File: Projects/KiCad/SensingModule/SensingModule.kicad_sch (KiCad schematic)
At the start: 38 parts, among them J1 Conn_01x05_Socket, J2 Conn_01x02_Pin, J3 Conn_01x05_Pin, J4 Micro_SD_Card_Det_Hirose_DM3AT, SW1 SW_Push, SW2 SW_Push, U2 NUCLEO-F303K8, U4 MCP2562-E-P, U5 TLP222A, U6 MB85RS2MT, U7 MB85RS2MT

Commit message: 抵抗値を調整
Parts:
- R12, R13: value 100Ω -> 300Ω
- R14: value 1kΩ -> 300Ω
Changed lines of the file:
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@@
       (effects (font (size 1.27 1.27)) (justify left))
     )
-    (property "Value" "100Ω" (at 255.27 49.5299 0)
+    (property "Value" "300Ω" (at 255.27 49.5299 0)
       (effects (font (size 1.27 1.27)) (justify left))
     )
@@
       (effects (font (size 1.27 1.27)) (justify left))
     )
-    (property "Value" "100Ω" (at 245.11 49.5299 0)
+    (property "Value" "300Ω" (at 245.11 49.5299 0)
       (effects (font (size 1.27 1.27)) (justify left))
     )
@@
       (effects (font (size 1.27 1.27)) (justify left))
     )
-    (property "Value" "1kΩ" (at 265.43 49.5299 0)
-      (effects (font (size 1.27 1.27)) (justify left))
-    )
+    (property "Value" "300Ω" (at 265.43 49.5299 0)
+      (effects (font (size 1.27 1.27)) (justify left))
+    )

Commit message: リセッタブルフューズをSMDに変更
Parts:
- F1: footprint Fuse:Fuse_BelFuse_0ZRE0005FF_L8.3mm_W3.8mm -> Fuse:Fuse_1206_3216Metric_Pad1.42x1.75mm_HandSolder
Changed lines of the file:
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@@
       (effects (font (size 1.27 1.27)))
     )
-    (property "Footprint" "Fuse:Fuse_BelFuse_0ZRE0005FF_L8.3mm_W3.8mm" (at 154.94 74.93 0)
+    (property "Footprint" "Fuse:Fuse_1206_3216Metric_Pad1.42x1.75mm_HandSolder" (at 154.94 74.93 0)
       (effects (font (size 1.27 1.27)) (justify left) hide)
     )

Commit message: 一通り部品を選定
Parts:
- D1, D2: value LED -> ORANGE
- D3, D4: value LED -> GREEN
- D5, D6: value LED -> RED
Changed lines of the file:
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@@
       (effects (font (size 1.27 1.27)) (justify right))
     )
-    (property "Value" "LED" (at 256.54 61.2774 90)
+    (property "Value" "GREEN" (at 256.54 61.2774 90)
       (effects (font (size 1.27 1.27)) (justify right))
     )
@@
       (effects (font (size 1.27 1.27)) (justify right))
     )
-    (property "Value" "LED" (at 246.38 61.2774 90)
+    (property "Value" "GREEN" (at 246.38 61.2774 90)
       (effects (font (size 1.27 1.27)) (justify right))
     )
@@
       (effects (font (size 1.27 1.27)) (justify right))
     )
-    (property "Value" "LED" (at 276.86 61.2774 90)
+    (property "Value" "RED" (at 276.86 61.2774 90)
       (effects (font (size 1.27 1.27)) (justify right))
     )
@@
       (effects (font (size 1.27 1.27)) (justify right))
     )
-    (property "Value" "LED" (at 226.06 61.2774 90)
+    (property "Value" "ORANGE" (at 226.06 61.2774 90)
       (effects (font (size 1.27 1.27)) (justify right))
     )
@@
       (effects (font (size 1.27 1.27)) (justify right))
     )
-    (property "Value" "LED" (at 236.22 61.2774 90)
+    (property "Value" "ORANGE" (at 236.22 61.2774 90)
       (effects (font (size 1.27 1.27)) (justify right))
     )
@@
       (effects (font (size 1.27 1.27)) (justify right))
     )
-    (property "Value" "LED" (at 266.7 61.2774 90)
-      (effects (font (size 1.27 1.27)) (justify right))
-    )
+    (property "Value" "RED" (at 266.7 61.2774 90)
+      (effects (font (size 1.27 1.27)) (justify right))
+    )

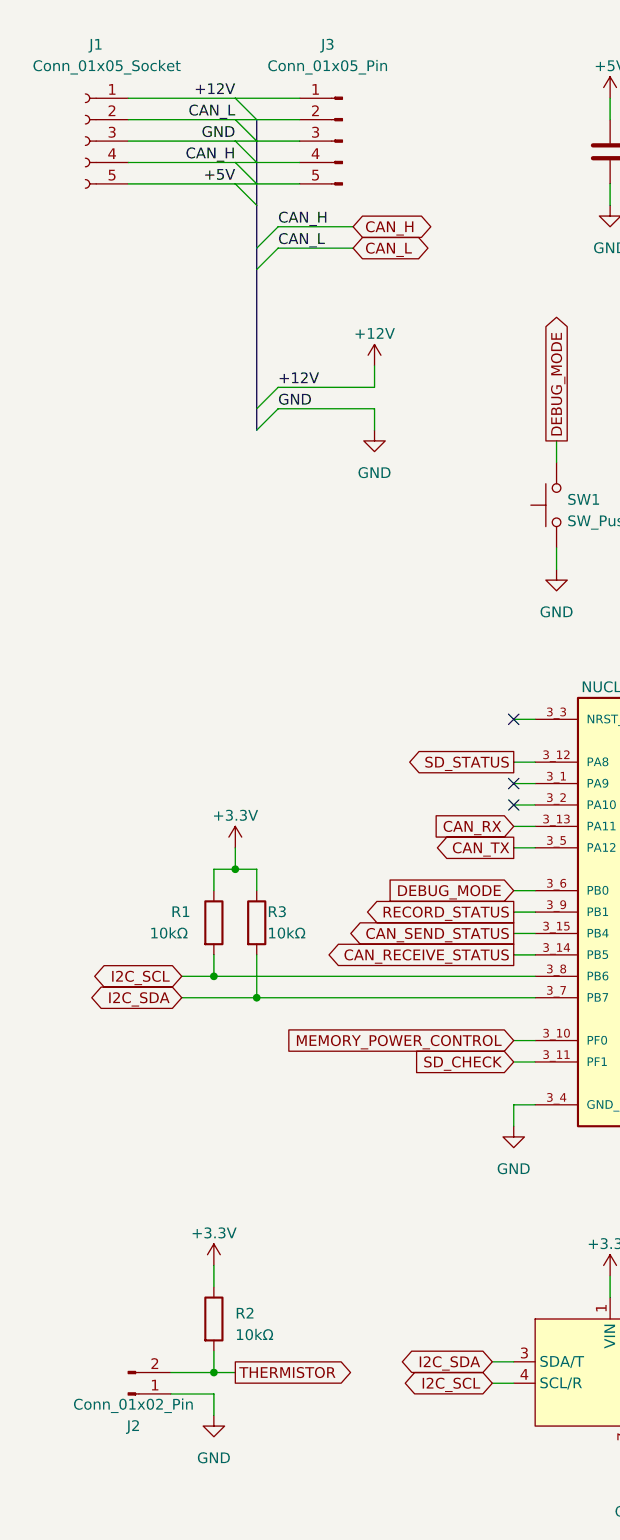
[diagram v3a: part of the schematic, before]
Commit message: 計測モジュールとフライトモジュールのコネクタを再配置
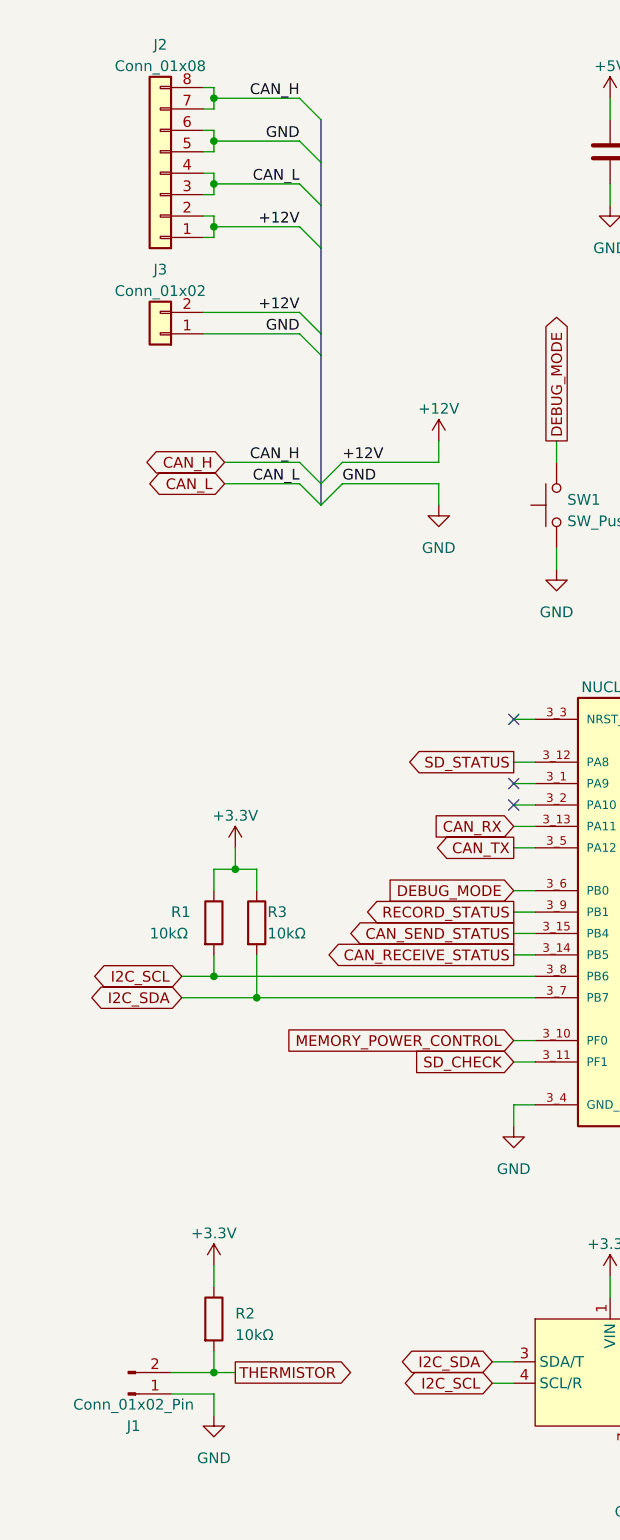
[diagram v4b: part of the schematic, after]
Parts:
- removed J1: Conn_01x05_Socket, Connector_PinSocket_2.54mm:PinSocket_1x05_P2.54mm_Vertical, symbol Connector:Conn_01x05_Socket
- removed J3: Conn_01x05_Pin, Connector_PinHeader_2.54mm:PinHeader_1x05_P2.54mm_Vertical, symbol Connector:Conn_01x05_Pin
- added J2: Conn_01x08, Connector_Hirose:Hirose_DF11-8DP-2DSA_2x04_P2.00mm_Vertical, symbol Connector_Generic:Conn_01x08
- added J3: Conn_01x02, Hirose_Connector:Hirose_DF1B, symbol Connector_Generic:Conn_01x02
- renumbered J2 to J1
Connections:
- net +12V: now also J2.1 (Pin_1), J2.2 (Pin_2), J3.2 (Pin_2)
- net CAN_H: now also J2.7 (Pin_7), J2.8 (Pin_8)
- net CAN_L: now also J2.3 (Pin_3), J2.4 (Pin_4)
- net GND: now also J2.5 (Pin_5), J2.6 (Pin_6), J3.1 (Pin_1)

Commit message: 基板設計の都市伝説をいろいろ適応
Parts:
- U5: renamed from U2; footprint MODULE_NUCLEO-F303K8 -> NUCLEO-F303K8:MODULE_NUCLEO-F303K8
- renumbered D6 to D3, D5 to D4, D3 to D5, D4 to D6, J3 to J1, J1 to J3, R8 to R1, R14 to R10, R12 to R11, R11 to R12, R10 to R13, R5 to R14, R13 to R15, R4 to R2, R9 to R3, R3 to R4, R1 to R5, R7 to R6, R15 to R7, R6 to R8, R2 to R9, U4 to U1, U3 to U2, U1 to U3, U5 to U4, U7 to U6, U6 to U7

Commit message: テストポイントを追加
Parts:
- added TP1, TP2, TP3: TestPoint, Connector_Pin:Pin_D1.0mm_L10.0mm, symbol Connector:TestPoint
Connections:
- net CAN_H: now also TP1.1
- net CAN_L: now also TP2.1
- net MEMORY_POWER: now also TP3.1
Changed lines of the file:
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@@
+    )
+  )
+  (symbol (lib_id "Connector:TestPoint") (at 156.21 64.77 90) (unit 1)
+    (in_bom yes) (on_board yes) (dnp no) (fields_autoplaced)
+    (property "Reference" "TP3" (at 152.908 59.69 90)
+      (effects (font (size 1.27 1.27)))
+    )
+    (property "Value" "TestPoint" (at 152.908 62.23 90)
+      (effects (font (size 1.27 1.27)))
+    )
+    (property "Footprint" "Connector_Pin:Pin_D1.0mm_L10.0mm" (at 156.21 59.69 0)
+      (effects (font (size 1.27 1.27)) hide)
+    )
+    (property "Datasheet" "~" (at 156.21 59.69 0)
+      (effects (font (size 1.27 1.27)) hide)
+    )
+    (pin "1")
+    (instances
+      (project "SensingModule"
+        (path "/ea1ed597-7cd3-4340-902e-bdce8f2d7a62"
+          (reference "TP3") (unit 1)
+        )
+      )
     )
   )
@@
         (path "/ea1ed597-7cd3-4340-902e-bdce8f2d7a62"
           (reference "#PWR016") (unit 1)
+        )
+      )
+    )
+  )
+  (symbol (lib_id "Connector:TestPoint") (at 116.84 39.37 180) (unit 1)
+    (in_bom yes) (on_board yes) (dnp no) (fields_autoplaced)
+    (property "Reference" "TP2" (at 119.38 42.037 0)
+      (effects (font (size 1.27 1.27)) (justify right))
+    )
+    (property "Value" "TestPoint" (at 119.38 44.577 0)
+      (effects (font (size 1.27 1.27)) (justify right))
+    )
+    (property "Footprint" "Connector_Pin:Pin_D1.0mm_L10.0mm" (at 111.76 39.37 0)
+      (effects (font (size 1.27 1.27)) hide)
+    )
+    (property "Datasheet" "~" (at 111.76 39.37 0)
+      (effects (font (size 1.27 1.27)) hide)
+    )
+    (pin "1")
+    (instances
+      (project "SensingModule"
+        (path "/ea1ed597-7cd3-4340-902e-bdce8f2d7a62"
+          (reference "TP2") (unit 1)
         )
       )
@@
         )
       )
+    )
+  )
+  (symbol (lib_id "Connector:TestPoint") (at 116.84 31.75 0) (unit 1)
+    (in_bom yes) (on_board yes) (dnp no) (fields_autoplaced)
+    (property "Reference" "TP1" (at 119.38 27.813 0)
+      (effects (font (size 1.27 1.27)) (justify left))
+    )
+    (property "Value" "TestPoint" (at 119.38 30.353 0)
+      (effects (font (size 1.27 1.27)) (justify left))
+    )
+    (property "Footprint" "Connector_Pin:Pin_D1.0mm_L10.0mm" (at 121.92 31.75 0)
+      (effects (font (size 1.27 1.27)) hide)
+    )
+    (property "Datasheet" "~" (at 121.92 31.75 0)
+      (effects (font (size 1.27 1.27)) hide)
+    )
+    (pin "1")
+    (instances
+      (project "SensingModule"
+        (path "/ea1ed597-7cd3-4340-902e-bdce8f2d7a62"
+          (reference "TP1") (unit 1)
+        )
+      )

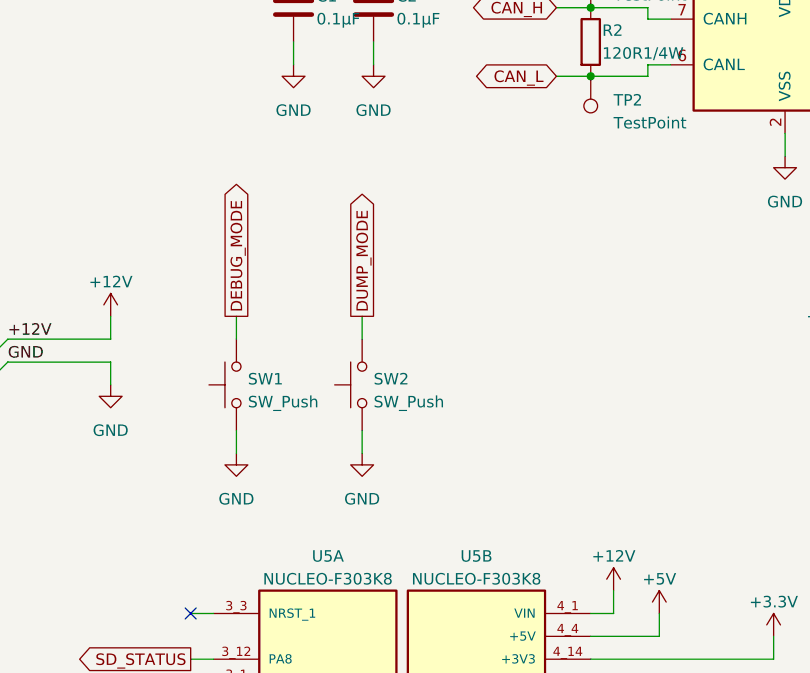
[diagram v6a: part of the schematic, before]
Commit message: スイッチをピアノスイッチに変更
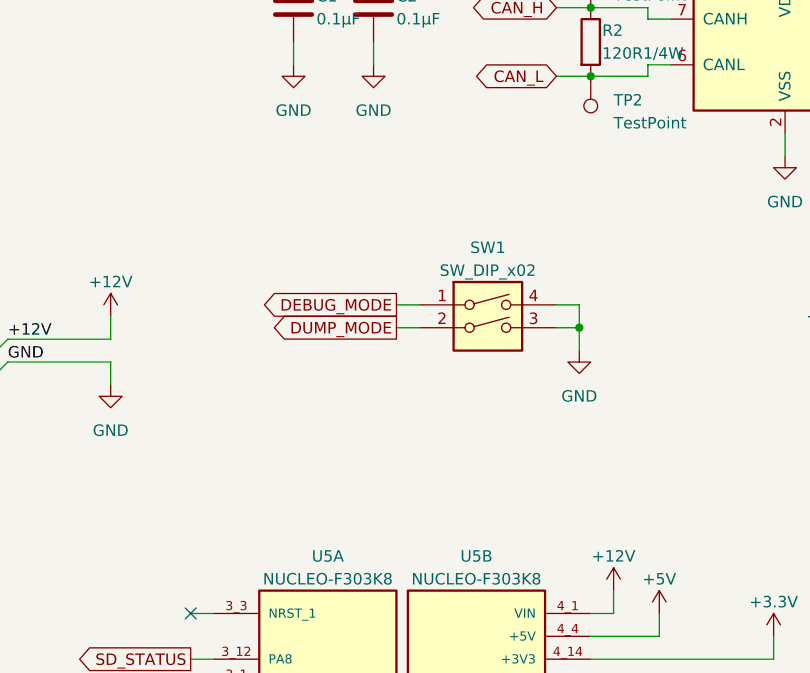
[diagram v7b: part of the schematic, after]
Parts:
- removed SW1, SW2: SW_Push, Button_Switch_THT:SW_PUSH_6mm, symbol Switch:SW_Push
- added SW1: SW_DIP_x02, Button_Switch_THT:SW_DIP_SPSTx02_Piano_10.8x6.64mm_W7.62mm_P2.54mm, symbol Switch:SW_DIP_x02
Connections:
- net DEBUG_MODE: now also SW1.1
- net DUMP_MODE: now also SW1.2
- net GND: now also SW1.3, SW1.4
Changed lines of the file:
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@@
   (junction (at 181.61 71.12) (diameter 0) (color 0 0 0 0)
+  )
+  (junction (at 115.57 67.31) (diameter 0) (color 0 0 0 0)
   )
   (junction (at 36.83 129.54) (diameter 0) (color 0 0 0 0)
@@
     (stroke (width 0) (type default))
   )
-  (wire (pts (xy 77.47 66.04) (xy 77.47 68.58))
-    (stroke (width 0) (type default))
-  )
   (wire (pts (xy 83.82 25.4) (xy 83.82 27.94))
     (stroke (width 0) (type default))
@@
     (stroke (width 0) (type default))
   )
-  (wire (pts (xy 91.44 66.04) (xy 91.44 68.58))
-    (stroke (width 0) (type default))
-  )
   (wire (pts (xy 41.91 132.08) (xy 74.93 132.08))
     (stroke (width 0) (type default))
@@
     (stroke (width 0) (type default))
   )
+  (wire (pts (xy 95.25 67.31) (xy 97.79 67.31))
+    (stroke (width 0) (type default))
+  )
   (wire (pts (xy 83.82 165.1) (xy 83.82 167.64))
     (stroke (width 0) (type default))
@@
     (stroke (width 0) (type default))
   )
+  (wire (pts (xy 113.03 67.31) (xy 115.57 67.31))
+    (stroke (width 0) (type default))
+  )
   (wire (pts (xy 123.19 33.02) (xy 123.19 31.75))
     (stroke (width 0) (type default))
@@
     (stroke (width 0) (type default))
   )
+  (wire (pts (xy 115.57 67.31) (xy 115.57 69.85))
+    (stroke (width 0) (type default))
+  )
   (wire (pts (xy 167.64 124.46) (xy 170.18 124.46))
     (stroke (width 0) (type default))
@@
     (stroke (width 0) (type default))
   )
+  (wire (pts (xy 115.57 64.77) (xy 115.57 67.31))
+    (stroke (width 0) (type default))
+  )
   (wire (pts (xy 46.99 71.12) (xy 38.1 71.12))
     (stroke (width 0) (type default))
@@
     (stroke (width 0) (type default))
   )
+  (wire (pts (xy 95.25 64.77) (xy 97.79 64.77))
+    (stroke (width 0) (type default))
+  )
   (wire (pts (xy 100.33 179.07) (xy 102.87 179.07))
     (stroke (width 0) (type default))
@@
     (stroke (width 0) (type default))
   )
-  (wire (pts (xy 91.44 78.74) (xy 91.44 81.28))
-    (stroke (width 0) (type default))
-  )
   (wire (pts (xy 184.15 58.42) (xy 181.61 58.42))
     (stroke (width 0) (type default))
@@
     (stroke (width 0) (type default))
   )
-  (wire (pts (xy 77.47 78.74) (xy 77.47 81.28))
-    (stroke (width 0) (type default))
-  )
   (wire (pts (xy 245.11 142.24) (xy 245.11 144.78))
     (stroke (width 0) (type default))
@@
   )
   (wire (pts (xy 36.83 35.56) (xy 46.99 35.56))
+    (stroke (width 0) (type default))
+  )
+  (wire (pts (xy 113.03 64.77) (xy 115.57 64.77))
     (stroke (width 0) (type default))
   )
@@
     )
   )
-  (global_label "DUMP_MODE" (shape output) (at 91.44 66.04 90) (fields_autoplaced)
-    (effects (font (size 1.27 1.27)) (justify left))
-    (property "Intersheetrefs" "${INTERSHEET_REFS}" (at 91.44 51.6438 90)
-      (effects (font (size 1.27 1.27)) (justify left) hide)
-    )
-  )
   (global_label "MEMORY_POWER_CONTROL" (shape input) (at 184.15 58.42 0) (fields_autoplaced)
     (effects (font (size 1.27 1.27)) (justify left))
@@
     )
   )
+  (global_label "DUMP_MODE" (shape output) (at 95.25 67.31 180) (fields_autoplaced)
+    (effects (font (size 1.27 1.27)) (justify right))
+    (property "Intersheetrefs" "${INTERSHEET_REFS}" (at 80.8538 67.31 0)
+      (effects (font (size 1.27 1.27)) (justify right) hide)
+    )
+  )
   (global_label "SPI_SCLK" (shape input) (at 270.51 102.87 0) (fields_autoplaced)
     (effects (font (size 1.27 1.27)) (justify left))
@@
     )
   )
+  (global_label "DEBUG_MODE" (shape output) (at 95.25 64.77 180) (fields_autoplaced)
+    (effects (font (size 1.27 1.27)) (justify right))
+    (property "Intersheetrefs" "${INTERSHEET_REFS}" (at 79.8862 64.77 0)
+      (effects (font (size 1.27 1.27)) (justify right) hide)
+    )
+  )
   (global_label "CAN_RX" (shape output) (at 153.67 33.02 0) (fields_autoplaced)
     (effects (font (size 1.27 1.27)) (justify left))
@@
     )
   )
-  (global_label "DEBUG_MODE" (shape output) (at 77.47 66.04 90) (fields_autoplaced)
-    (effects (font (size 1.27 1.27)) (justify left))
-    (property "Intersheetrefs" "${INTERSHEET_REFS}" (at 77.47 50.6762 90)
-      (effects (font (size 1.27 1.27)) (justify left) hide)
-    )
-  )
   (global_label "THERMISTOR" (shape output) (at 39.37 176.53 0) (fields_autoplaced)
     (effects (font (size 1.27 1.27)) (justify left))
@@
     )
   )
+  (symbol (lib_id "Switch:SW_DIP_x02") (at 105.41 67.31 0) (unit 1)
+    (in_bom yes) (on_board yes) (dnp no) (fields_autoplaced)
+    (property "Reference" "SW1" (at 105.41 58.42 0)
+      (effects (font (size 1.27 1.27)))
+    )
+    (property "Value" "SW_DIP_x02" (at 105.41 60.96 0)
+      (effects (font (size 1.27 1.27)))
+    )
+    (property "Footprint" "Button_Switch_THT:SW_DIP_SPSTx02_Piano_10.8x6.64mm_W7.62mm_P2.54mm" (at 105.41 67.31 0)
+      (effects (font (size 1.27 1.27)) hide)
+    )
+    (property "Datasheet" "~" (at 105.41 67.31 0)
+      (effects (font (size 1.27 1.27)) hide)
+    )
+    (pin "1")
+    (pin "2")
+    (pin "3")
+    (pin "4")
+    (instances
+      (project "SensingModule"
+        (path "/ea1ed597-7cd3-4340-902e-bdce8f2d7a62"
+          (reference "SW1") (unit 1)
+        )
+      )
+    )
+  )
   (symbol (lib_id "Device:LED") (at 252.73 58.42 90) (unit 1)
     (in_bom yes) (on_board yes) (dnp no) (fields_autoplaced)
@@
         (path "/ea1ed597-7cd3-4340-902e-bdce8f2d7a62"
           (reference "#PWR026") (unit 1)
-        )
-      )
-    )
-  )
-  (symbol (lib_id "Switch:SW_Push") (at 91.44 73.66 90) (unit 1)
-    (in_bom yes) (on_board yes) (dnp no) (fields_autoplaced)
-    (property "Reference" "SW2" (at 92.71 73.025 90)
-      (effects (font (size 1.27 1.27)) (justify right))
-    )
-    (property "Value" "SW_Push" (at 92.71 75.565 90)
-      (effects (font (size 1.27 1.27)) (justify right))
-    )
-    (property "Footprint" "Button_Switch_THT:SW_PUSH_6mm" (at 86.36 73.66 0)
-      (effects (font (size 1.27 1.27)) hide)
-    )
-    (property "Datasheet" "~" (at 86.36 73.66 0)
-      (effects (font (size 1.27 1.27)) hide)
-    )
-    (pin "1")
-    (pin "2")
-    (instances
-      (project "SensingModule"
-        (path "/ea1ed597-7cd3-4340-902e-bdce8f2d7a62"
-          (reference "SW2") (unit 1)
         )
       )
@@
     )
   )
+  (symbol (lib_id "power:GND") (at 115.57 69.85 0) (mirror y) (unit 1)
+    (in_bom yes) (on_board yes) (dnp no) (fields_autoplaced)
+    (property "Reference" "#PWR044" (at 115.57 76.2 0)
+      (effects (font (size 1.27 1.27)) hide)
+    )
+    (property "Value" "GND" (at 115.57 74.93 0)
+      (effects (font (size 1.27 1.27)))
+    )
+    (property "Footprint" "" (at 115.57 69.85 0)
+      (effects (font (size 1.27 1.27)) hide)
+    )
+    (property "Datasheet" "" (at 115.57 69.85 0)
+      (effects (font (size 1.27 1.27)) hide)
+    )
+    (pin "1")
+    (instances
+      (project "SensingModule"
+        (path "/ea1ed597-7cd3-4340-902e-bdce8f2d7a62"
+          (reference "#PWR044") (unit 1)
+        )
+      )
+    )
+  )
   (symbol (lib_id "Device:R") (at 262.89 48.26 0) (unit 1)
     (in_bom yes) (on_board yes) (dnp no) (fields_autoplaced)
@@
         (path "/ea1ed597-7cd3-4340-902e-bdce8f2d7a62"
           (reference "#PWR025") (unit 1)
-        )
-      )
-    )
-  )
-  (symbol (lib_id "Switch:SW_Push") (at 77.47 73.66 90) (unit 1)
-    (in_bom yes) (on_board yes) (dnp no) (fields_autoplaced)
-    (property "Reference" "SW1" (at 78.74 73.025 90)
-      (effects (font (size 1.27 1.27)) (justify right))
-    )
-    (property "Value" "SW_Push" (at 78.74 75.565 90)
-      (effects (font (size 1.27 1.27)) (justify right))
-    )
-    (property "Footprint" "Button_Switch_THT:SW_PUSH_6mm" (at 72.39 73.66 0)
-      (effects (font (size 1.27 1.27)) hide)
-    )
-    (property "Datasheet" "~" (at 72.39 73.66 0)
-      (effects (font (size 1.27 1.27)) hide)
-    )
-    (pin "1")
-    (pin "2")
-    (instances
-      (project "SensingModule"
-        (path "/ea1ed597-7cd3-4340-902e-bdce8f2d7a62"
-          (reference "SW1") (unit 1)
         )
       )
@@
     )
   )
-  (symbol (lib_id "power:GND") (at 91.44 81.28 0) (mirror y) (unit 1)
-    (in_bom yes) (on_board yes) (dnp no) (fields_autoplaced)
-    (property "Reference" "#PWR012" (at 91.44 87.63 0)
-      (effects (font (size 1.27 1.27)) hide)
-    )
-    (property "Value" "GND" (at 91.44 86.36 0)
-      (effects (font (size 1.27 1.27)))
-    )
-    (property "Footprint" "" (at 91.44 81.28 0)
-      (effects (font (size 1.27 1.27)) hide)
-    )
-    (property "Datasheet" "" (at 91.44 81.28 0)
-      (effects (font (size 1.27 1.27)) hide)
-    )
-    (pin "1")
-    (instances
-      (project "SensingModule"
-        (path "/ea1ed597-7cd3-4340-902e-bdce8f2d7a62"
-          (reference "#PWR012") (unit 1)
-        )
-      )
-    )
-  )
   (symbol (lib_id "Device:LED") (at 232.41 58.42 90) (unit 1)
     (in_bom yes) (on_board yes) (dnp no) (fields_autoplaced)
@@
         )
       )
-    )
-  )
-  (symbol (lib_id "power:GND") (at 77.47 81.28 0) (mirror y) (unit 1)
-    (in_bom yes) (on_board yes) (dnp no) (fields_autoplaced)
-    (property "Reference" "#PWR07" (at 77.47 87.63 0)
-      (effects (font (size 1.27 1.27)) hide)
-    )
-    (property "Value" "GND" (at 77.47 86.36 0)
-      (effects (font (size 1.27 1.27)))
-    )
-    (property "Footprint" "" (at 77.47 81.28 0)
-      (effects (font (size 1.27 1.27)) hide)
-    )
-    (property "Datasheet" "" (at 77.47 81.28 0)
-      (effects (font (size 1.27 1.27)) hide)
-    )
-    (pin "1")
-    (instances
-      (project "SensingModule"
-        (path "/ea1ed597-7cd3-4340-902e-bdce8f2d7a62"
-          (reference "#PWR07") (unit 1)
-        )
-      )
